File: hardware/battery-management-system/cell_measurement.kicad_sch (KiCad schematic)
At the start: 25 parts, among them Q10 DMN3404L, Q11 BS250FTA, Q12 BS250FTA, Q13 BS250FTA, Q14 BS250FTA, Q15 BS250FTA, Q9 DMN3404L, U11 LM2904M8-13, U12 LM2904M8-13

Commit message: fix design errors
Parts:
- added C34, C35, C36, C37: 100nF, benediktibk:C_0603_1608Metric_Pad1.08x0.95mm_HandSolder, symbol benediktibk:C_100nF_SMD_0603_50V
- renumbered C31 to C30, C32 to C31, C33 to C32, C34 to C33, R42 to R33, R43 to R34, R44 to R35, R45 to R36, R46 to R37, R47 to R38, R48 to R39, R49 to R40, R50 to R41, R51 to R42, R52 to R43, R53 to R44, U11 to U10, U12 to U11
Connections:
- net CELL1: now also C37.1
- net CELL2: now also C36.1
- net CELL3: now also C35.1
- net CELL4: now also C34.1
- net GND: now also C34.2, C35.2, C36.2, C37.2

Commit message: fix design errors
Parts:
- renumbered U11 to U10, U10 to U9
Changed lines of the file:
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@@
   (symbol (lib_id "benediktibk:LM2904M8-13") (at 177.8 109.22 0) (unit 1)
     (in_bom yes) (on_board yes) (dnp no) (fields_autoplaced)
-    (property "Reference" "U10" (at 177.8 99.06 0)
+    (property "Reference" "U9" (at 177.8 99.06 0)
       (effects (font (size 1.27 1.27)))
     )
@@
       (project "battery-management-system"
         (path "/5272f0ff-3069-41a9-bca2-80beede8b4b2/3d1e17ba-3c41-4767-81ce-6010cdb0d005"
-          (reference "U10") (unit 1)
+          (reference "U9") (unit 1)
         )
       )
@@
   (symbol (lib_id "benediktibk:LM2904M8-13") (at 83.82 30.48 0) (unit 3)
     (in_bom yes) (on_board yes) (dnp no)
-    (property "Reference" "U10" (at 82.55 29.2099 0)
+    (property "Reference" "U9" (at 82.55 29.2099 0)
       (effects (font (size 1.27 1.27)) (justify left))
     )
@@
       (project "battery-management-system"
         (path "/5272f0ff-3069-41a9-bca2-80beede8b4b2/3d1e17ba-3c41-4767-81ce-6010cdb0d005"
-          (reference "U10") (unit 3)
+          (reference "U9") (unit 3)
         )
       )
@@
   (symbol (lib_id "benediktibk:LM2904M8-13") (at 125.73 30.48 0) (unit 3)
     (in_bom yes) (on_board yes) (dnp no) (fields_autoplaced)
-    (property "Reference" "U11" (at 124.46 29.2099 0)
+    (property "Reference" "U10" (at 124.46 29.2099 0)
       (effects (font (size 1.27 1.27)) (justify left))
     )
@@
       (project "battery-management-system"
         (path "/5272f0ff-3069-41a9-bca2-80beede8b4b2/3d1e17ba-3c41-4767-81ce-6010cdb0d005"
-          (reference "U11") (unit 3)
+          (reference "U10") (unit 3)
         )
       )
@@
   (symbol (lib_id "benediktibk:LM2904M8-13") (at 177.8 128.27 0) (unit 1)
     (in_bom yes) (on_board yes) (dnp no) (fields_autoplaced)
-    (property "Reference" "U11" (at 177.8 118.11 0)
+    (property "Reference" "U10" (at 177.8 118.11 0)
       (effects (font (size 1.27 1.27)))
     )
@@
       (project "battery-management-system"
         (path "/5272f0ff-3069-41a9-bca2-80beede8b4b2/3d1e17ba-3c41-4767-81ce-6010cdb0d005"
-          (reference "U11") (unit 1)
+          (reference "U10") (unit 1)
         )
       )
@@
   (symbol (lib_id "benediktibk:LM2904M8-13") (at 177.8 69.85 0) (unit 2)
     (in_bom yes) (on_board yes) (dnp no) (fields_autoplaced)
-    (property "Reference" "U10" (at 177.8 59.69 0)
+    (property "Reference" "U9" (at 177.8 59.69 0)
       (effects (font (size 1.27 1.27)))
     )
@@
       (project "battery-management-system"
         (path "/5272f0ff-3069-41a9-bca2-80beede8b4b2/3d1e17ba-3c41-4767-81ce-6010cdb0d005"
-          (reference "U10") (unit 2)
+          (reference "U9") (unit 2)
         )
       )
@@
   (symbol (lib_id "benediktibk:LM2904M8-13") (at 177.8 90.17 0) (unit 2)
     (in_bom yes) (on_board yes) (dnp no)
-    (property "Reference" "U11" (at 177.8 80.01 0)
+    (property "Reference" "U10" (at 177.8 80.01 0)
       (effects (font (size 1.27 1.27)))
     )
@@
       (project "battery-management-system"
         (path "/5272f0ff-3069-41a9-bca2-80beede8b4b2/3d1e17ba-3c41-4767-81ce-6010cdb0d005"
-          (reference "U11") (unit 2)
-        )
-      )
+          (reference "U10") (unit 2)
+        )
+      )

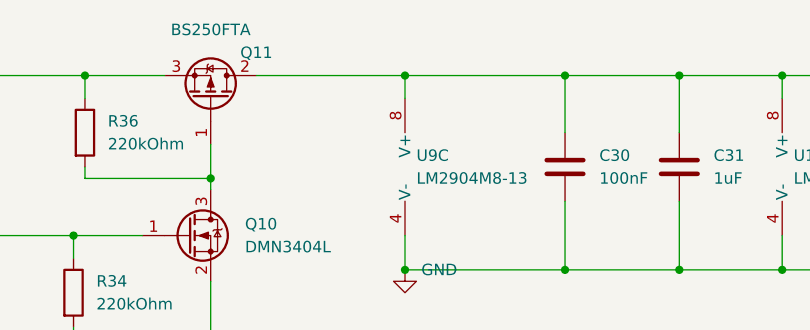
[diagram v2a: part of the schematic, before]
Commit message: add heatsink and fix ERC errors
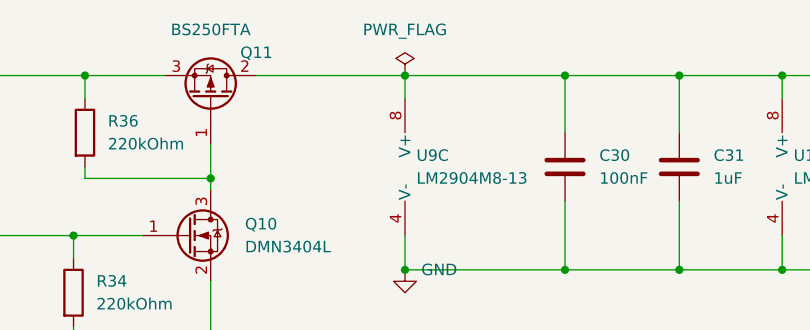
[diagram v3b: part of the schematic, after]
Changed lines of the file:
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@@
+    )
+  )
+  (symbol (lib_id "power:PWR_FLAG") (at 81.28 20.32 0) (unit 1)
+    (in_bom yes) (on_board yes) (dnp no) (fields_autoplaced)
+    (property "Reference" "#FLG09" (at 81.28 18.415 0)
+      (effects (font (size 1.27 1.27)) hide)
+    )
+    (property "Value" "PWR_FLAG" (at 81.28 15.24 0)
+      (effects (font (size 1.27 1.27)))
+    )
+    (property "Footprint" "" (at 81.28 20.32 0)
+      (effects (font (size 1.27 1.27)) hide)
+    )
+    (property "Datasheet" "~" (at 81.28 20.32 0)
+      (effects (font (size 1.27 1.27)) hide)
+    )
+    (pin "1")
+    (instances
+      (project "battery-management-system"
+        (path "/5272f0ff-3069-41a9-bca2-80beede8b4b2/3d1e17ba-3c41-4767-81ce-6010cdb0d005"
+          (reference "#FLG09") (unit 1)
+        )
+      )
     )
   )

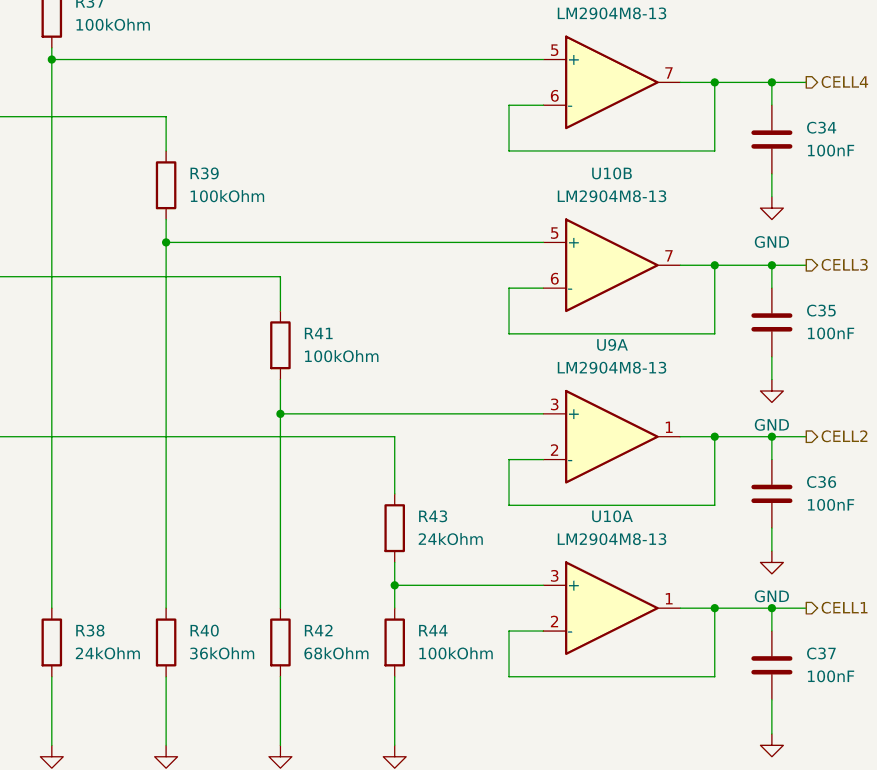
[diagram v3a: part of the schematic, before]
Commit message: layout BMS R02
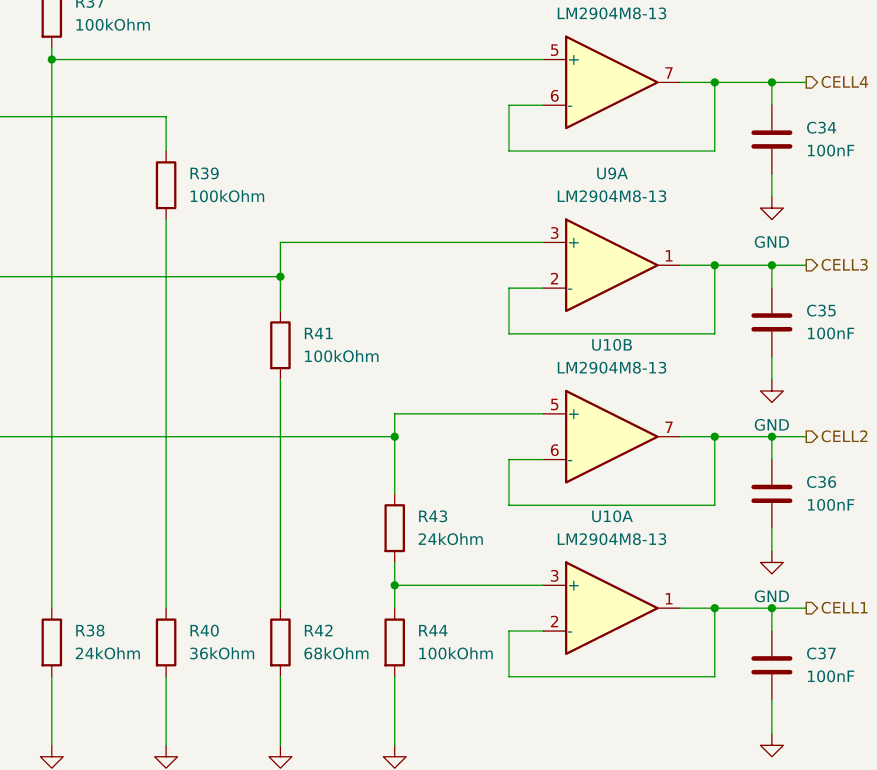
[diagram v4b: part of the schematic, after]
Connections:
- net CELL2: now also U10.6 (-), U10.7; no longer U9.1, U9.2 (-)
- net CELL3: now also U9.1, U9.2 (-); no longer U10.6 (-), U10.7
- net at Q15.2 (D), R43.1: now also U10.5 (+)
- net at R39.2, R40.1: no longer U10.5 (+)
- net at R41.2, R42.1: no longer U9.3 (+)
- net at Q14.2 (D), R41.1: now also U9.3 (+)
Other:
- moved on the sheet: U10B, U9A
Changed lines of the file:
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@@
   (junction (at 195.58 90.17) (diameter 0) (color 0 0 0 0)
   )
-  (junction (at 140.97 106.68) (diameter 0) (color 0 0 0 0)
+  (junction (at 189.23 90.17) (diameter 0) (color 0 0 0 0)
+  )
+  (junction (at 115.57 67.31) (diameter 0) (color 0 0 0 0)
+  )
+  (junction (at 67.31 81.28) (diameter 0) (color 0 0 0 0)
+  )
+  (junction (at 123.19 41.91) (diameter 0) (color 0 0 0 0)
+  )
+  (junction (at 111.76 20.32) (diameter 0) (color 0 0 0 0)
+  )
+  (junction (at 29.21 118.11) (diameter 0) (color 0 0 0 0)
+  )
+  (junction (at 99.06 41.91) (diameter 0) (color 0 0 0 0)
+  )
+  (junction (at 153.67 109.22) (diameter 0) (color 0 0 0 0)
+  )
+  (junction (at 99.06 20.32) (diameter 0) (color 0 0 0 0)
+  )
+  (junction (at 67.31 99.06) (diameter 0) (color 0 0 0 0)
+  )
+  (junction (at 189.23 69.85) (diameter 0) (color 0 0 0 0)
+  )
+  (junction (at 140.97 20.32) (diameter 0) (color 0 0 0 0)
+  )
+  (junction (at 45.72 20.32) (diameter 0) (color 0 0 0 0)
+  )
+  (junction (at 195.58 69.85) (diameter 0) (color 0 0 0 0)
+  )
+  (junction (at 195.58 128.27) (diameter 0) (color 0 0 0 0)
+  )
+  (junction (at 111.76 41.91) (diameter 0) (color 0 0 0 0)
+  )
+  (junction (at 189.23 128.27) (diameter 0) (color 0 0 0 0)
+  )
+  (junction (at 195.58 109.22) (diameter 0) (color 0 0 0 0)
+  )
+  (junction (at 44.45 99.06) (diameter 0) (color 0 0 0 0)
+  )
+  (junction (at 81.28 20.32) (diameter 0) (color 0 0 0 0)
+  )
+  (junction (at 81.28 41.91) (diameter 0) (color 0 0 0 0)
+  )
+  (junction (at 140.97 41.91) (diameter 0) (color 0 0 0 0)
+  )
+  (junction (at 123.19 20.32) (diameter 0) (color 0 0 0 0)
+  )
+  (junction (at 59.69 31.75) (diameter 0) (color 0 0 0 0)
+  )
+  (junction (at 140.97 91.44) (diameter 0) (color 0 0 0 0)
+  )
+  (junction (at 44.45 38.1) (diameter 0) (color 0 0 0 0)
   )
   (junction (at 189.23 109.22) (diameter 0) (color 0 0 0 0)
   )
-  (junction (at 115.57 67.31) (diameter 0) (color 0 0 0 0)
-  )
-  (junction (at 67.31 81.28) (diameter 0) (color 0 0 0 0)
-  )
-  (junction (at 123.19 41.91) (diameter 0) (color 0 0 0 0)
-  )
-  (junction (at 111.76 20.32) (diameter 0) (color 0 0 0 0)
-  )
-  (junction (at 29.21 118.11) (diameter 0) (color 0 0 0 0)
-  )
-  (junction (at 99.06 41.91) (diameter 0) (color 0 0 0 0)
-  )
-  (junction (at 99.06 20.32) (diameter 0) (color 0 0 0 0)
-  )
-  (junction (at 67.31 99.06) (diameter 0) (color 0 0 0 0)
-  )
-  (junction (at 189.23 69.85) (diameter 0) (color 0 0 0 0)
-  )
-  (junction (at 140.97 20.32) (diameter 0) (color 0 0 0 0)
-  )
-  (junction (at 45.72 20.32) (diameter 0) (color 0 0 0 0)
-  )
-  (junction (at 195.58 69.85) (diameter 0) (color 0 0 0 0)
-  )
-  (junction (at 195.58 128.27) (diameter 0) (color 0 0 0 0)
-  )
-  (junction (at 111.76 41.91) (diameter 0) (color 0 0 0 0)
-  )
-  (junction (at 189.23 128.27) (diameter 0) (color 0 0 0 0)
-  )
-  (junction (at 195.58 109.22) (diameter 0) (color 0 0 0 0)
-  )
-  (junction (at 44.45 99.06) (diameter 0) (color 0 0 0 0)
-  )
-  (junction (at 81.28 20.32) (diameter 0) (color 0 0 0 0)
-  )
-  (junction (at 81.28 41.91) (diameter 0) (color 0 0 0 0)
-  )
-  (junction (at 140.97 41.91) (diameter 0) (color 0 0 0 0)
-  )
-  (junction (at 123.19 20.32) (diameter 0) (color 0 0 0 0)
-  )
-  (junction (at 59.69 31.75) (diameter 0) (color 0 0 0 0)
-  )
-  (junction (at 44.45 38.1) (diameter 0) (color 0 0 0 0)
-  )
-  (junction (at 128.27 87.63) (diameter 0) (color 0 0 0 0)
-  )
-  (junction (at 189.23 90.17) (diameter 0) (color 0 0 0 0)
-  )
   (wire (pts (xy 44.45 95.25) (xy 44.45 99.06))
     (stroke (width 0) (type default))
@@
     (stroke (width 0) (type default))
   )
-  (wire (pts (xy 170.18 111.76) (xy 166.37 111.76))
-    (stroke (width 0) (type default))
-  )
   (wire (pts (xy 45.72 30.48) (xy 45.72 31.75))
     (stroke (width 0) (type default))
@@
     (stroke (width 0) (type default))
   )
-  (wire (pts (xy 128.27 87.63) (xy 128.27 128.27))
+  (wire (pts (xy 128.27 85.09) (xy 128.27 128.27))
     (stroke (width 0) (type default))
   )
@@
     (stroke (width 0) (type default))
   )
+  (wire (pts (xy 153.67 106.68) (xy 153.67 109.22))
+    (stroke (width 0) (type default))
+  )
   (wire (pts (xy 128.27 135.89) (xy 128.27 143.51))
     (stroke (width 0) (type default))
@@
     (stroke (width 0) (type default))
   )
-  (wire (pts (xy 128.27 87.63) (xy 170.18 87.63))
-    (stroke (width 0) (type default))
-  )
   (wire (pts (xy 195.58 90.17) (xy 195.58 92.71))
     (stroke (width 0) (type default))
@@
     (stroke (width 0) (type default))
   )
-  (wire (pts (xy 189.23 109.22) (xy 185.42 109.22))
+  (wire (pts (xy 166.37 111.76) (xy 170.18 111.76))
     (stroke (width 0) (type default))
   )
@@
     (stroke (width 0) (type default))
   )
+  (wire (pts (xy 166.37 92.71) (xy 170.18 92.71))
+    (stroke (width 0) (type default))
+  )
   (wire (pts (xy 67.31 62.23) (xy 67.31 81.28))
     (stroke (width 0) (type default))
   )
-  (wire (pts (xy 140.97 106.68) (xy 140.97 128.27))
-    (stroke (width 0) (type default))
-  )
   (wire (pts (xy 170.18 72.39) (xy 166.37 72.39))
     (stroke (width 0) (type default))
@@
     (stroke (width 0) (type default))
   )
-  (wire (pts (xy 140.97 102.87) (xy 140.97 106.68))
+  (wire (pts (xy 140.97 102.87) (xy 140.97 128.27))
     (stroke (width 0) (type default))
   )
@@
     (stroke (width 0) (type default))
   )
+  (wire (pts (xy 170.18 106.68) (xy 153.67 106.68))
+    (stroke (width 0) (type default))
+  )
   (wire (pts (xy 185.42 69.85) (xy 189.23 69.85))
     (stroke (width 0) (type default))
@@
     (stroke (width 0) (type default))
   )
+  (wire (pts (xy 185.42 109.22) (xy 189.23 109.22))
+    (stroke (width 0) (type default))
+  )
   (wire (pts (xy 64.77 20.32) (xy 81.28 20.32))
     (stroke (width 0) (type default))
@@
     (stroke (width 0) (type default))
   )
+  (wire (pts (xy 140.97 87.63) (xy 140.97 91.44))
+    (stroke (width 0) (type default))
+  )
+  (wire (pts (xy 185.42 90.17) (xy 189.23 90.17))
+    (stroke (width 0) (type default))
+  )
   (wire (pts (xy 44.45 87.63) (xy 44.45 82.55))
     (stroke (width 0) (type default))
@@
     (stroke (width 0) (type default))
   )
-  (wire (pts (xy 170.18 92.71) (xy 166.37 92.71))
-    (stroke (width 0) (type default))
-  )
   (wire (pts (xy 115.57 135.89) (xy 115.57 143.51))
     (stroke (width 0) (type default))
@@
     (stroke (width 0) (type default))
   )
-  (wire (pts (xy 128.27 85.09) (xy 128.27 87.63))
-    (stroke (width 0) (type default))
-  )
-  (wire (pts (xy 185.42 90.17) (xy 189.23 90.17))
-    (stroke (width 0) (type default))
-  )
   (wire (pts (xy 140.97 34.29) (xy 140.97 41.91))
     (stroke (width 0) (type default))
@@
     (stroke (width 0) (type default))
   )
-  (wire (pts (xy 140.97 106.68) (xy 170.18 106.68))
-    (stroke (width 0) (type default))
-  )
   (wire (pts (xy 22.86 82.55) (xy 44.45 82.55))
     (stroke (width 0) (type default))
@@
   )
   (wire (pts (xy 95.25 62.23) (xy 67.31 62.23))
+    (stroke (width 0) (type default))
+  )
+  (wire (pts (xy 170.18 87.63) (xy 140.97 87.63))
     (stroke (width 0) (type default))
   )
@@
     )
   )
-  (symbol (lib_id "benediktibk:LM2904M8-13") (at 177.8 109.22 0) (unit 1)
-    (in_bom yes) (on_board yes) (dnp no) (fields_autoplaced)
-    (property "Reference" "U9" (at 177.8 99.06 0)
-      (effects (font (size 1.27 1.27)))
-    )
-    (property "Value" "LM2904M8-13" (at 177.8 101.6 0)
-      (effects (font (size 1.27 1.27)))
-    )
-    (property "Footprint" "benediktibk:MSOP-8_3x3mm_P0.65mm" (at 177.8 109.22 0)
-      (effects (font (size 1.27 1.27)) hide)
-    )
-    (property "Datasheet" "" (at 177.8 109.22 0)
-      (effects (font (size 1.27 1.27)) hide)
-    )
-    (property "RS order number" "133-3375" (at 177.8 109.22 0)
+  (symbol (lib_id "benediktibk:LM2904M8-13") (at 177.8 90.17 0) (unit 1)
+    (in_bom yes) (on_board yes) (dnp no) (fields_autoplaced)
+    (property "Reference" "U9" (at 177.8 80.01 0)
+      (effects (font (size 1.27 1.27)))
+    )
+    (property "Value" "LM2904M8-13" (at 177.8 82.55 0)
+      (effects (font (size 1.27 1.27)))
+    )
+    (property "Footprint" "benediktibk:MSOP-8_3x3mm_P0.65mm" (at 177.8 90.17 0)
+      (effects (font (size 1.27 1.27)) hide)
+    )
+    (property "Datasheet" "" (at 177.8 90.17 0)
+      (effects (font (size 1.27 1.27)) hide)
+    )
+    (property "RS order number" "133-3375" (at 177.8 90.17 0)
       (effects (font (size 1.27 1.27)) hide)
     )
@@
     )
   )
-  (symbol (lib_id "benediktibk:LM2904M8-13") (at 177.8 90.17 0) (unit 2)
+  (symbol (lib_id "benediktibk:LM2904M8-13") (at 177.8 109.22 0) (unit 2)
     (in_bom yes) (on_board yes) (dnp no)
-    (property "Reference" "U10" (at 177.8 80.01 0)
-      (effects (font (size 1.27 1.27)))
-    )
-    (property "Value" "LM2904M8-13" (at 177.8 82.55 0)
-      (effects (font (size 1.27 1.27)))
-    )
-    (property "Footprint" "benediktibk:MSOP-8_3x3mm_P0.65mm" (at 177.8 90.17 0)
-      (effects (font (size 1.27 1.27)) hide)
-    )
-    (property "Datasheet" "" (at 177.8 90.17 0)
-      (effects (font (size 1.27 1.27)) hide)
-    )
-    (property "RS order number" "133-3375" (at 177.8 90.17 0)
-      (effects (font (size 1.27 1.27)) hide)
-    )
+    (property "Reference" "U10" (at 177.8 99.06 0)
+      (effects (font (size 1.27 1.27)))
+    )
+    (property "Value" "LM2904M8-13" (at 177.8 101.6 0)
+      (effects (font (size 1.27 1.27)))
+    )
+    (property "Footprint" "benediktibk:MSOP-8_3x3mm_P0.65mm" (at 177.8 109.22 0)
+      (effects (font (size 1.27 1.27)) hide)
+    )
+    (property "Datasheet" "" (at 177.8 109.22 0)
+      (effects (font (size 1.27 1.27)) hide)
+    )
+    (property "RS order number" "133-3375" (at 177.8 109.22 0)
+      (effects (font (size 1.27 1.27)) hide)
+    )

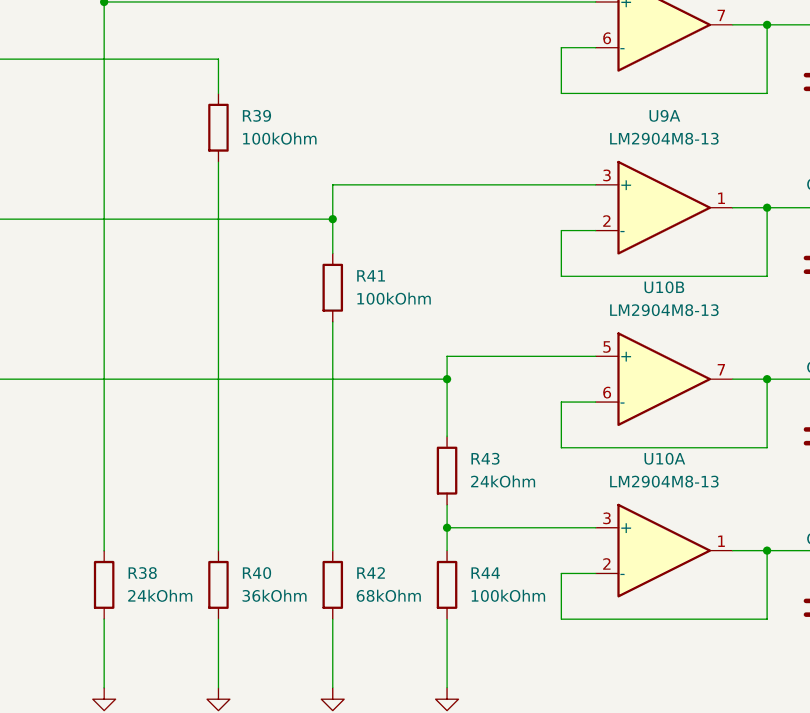
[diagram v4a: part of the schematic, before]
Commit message: fix cell voltage measurements
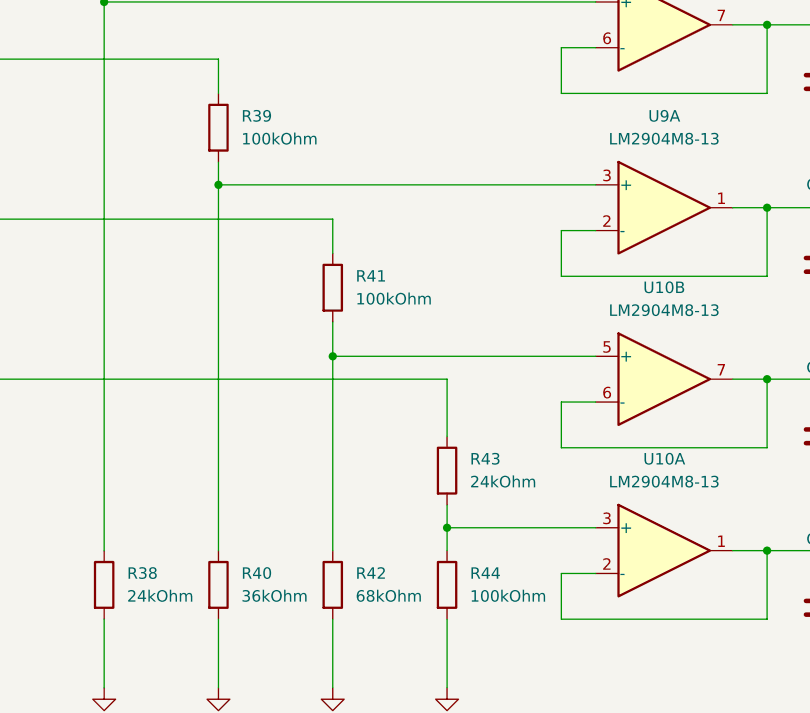
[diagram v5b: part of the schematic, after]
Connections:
- net at Q15.2 (D), R43.1: no longer U10.5 (+)
- net at R39.2, R40.1: now also U9.3 (+)
- net at Q14.2 (D), R41.1: no longer U9.3 (+)
- net at R41.2, R42.1: now also U10.5 (+)
